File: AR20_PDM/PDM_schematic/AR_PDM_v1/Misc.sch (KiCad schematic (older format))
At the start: 91 parts, among them SW1 SW_DIP_x07, SW2 SW_Push, U13 Fet-P, U14 Fet-P, U15 Fet-P, U16 Fet-P, U17 Fet-P, U18 Fet-P, U19 Fet-P, U20 Fet-P, U21 Fet-P, U22 Fet-P, U23 Fet-P, U24 Fet-P, U25 Fet-P, U26 Fet-P, U27 Fet-P, U28 Fet-P, U29 Fet-P, U30 Fet-P, U31 Fet-P

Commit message: Alpha version DONE! - Gerber files generated
- Tweeked
- checked and re cheked
- added all missing components
- Created a really nice silkscreen
- Ready To Test
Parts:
- removed SW2: SW_Push, Connector_JST:JST_EH_B2B-EH-A_1x02_P2.50mm_Vertical, symbol Switch:SW_Push
- added P1: B4B-PH-SM4-TB, AR_PDM_v1:JST_B4B-PH-SM4-TB, symbol AR20_PDM_v1-rescue:B4B-PH-SM4-TB
- added R88: somthing_K_something, Resistor_SMD:R_0603_1608Metric, symbol AR20_PDM_v1-rescue:R-Device
- D21: renamed from D23; value Shutdown_Circuit_Active -> Shutdown_Circuit_Supply
- renumbered D12 to D10, D13 to D11, D14 to D12, D15 to D13, D16 to D14, D17 to D15, D18 to D16, D19 to D17, D20 to D18, D21 to D19, D22 to D20, D31 to D22, D24 to D23, D25 to D24, D26 to D25, D27 to D26, D28 to D27, D29 to D28, D30 to D29, D7 to D5, D8 to D6, D9 to D7, D10 to D8, D11 to D9, R14 to R48, R15 to R49, R16 to R50, R17 to R51, R18 to R52, R19 to R53, R20 to R54, R21 to R55, R22 to R56, R23 to R57, R24 to R58, R25 to R59, R26 to R60, R27 to R61, R28 to R62, R29 to R63, R30 to R64, R31 to R65, R32 to R66, R33 to R67, R34 to R68, R35 to R69, R36 to R70, R37 to R71, R38 to R72, R39 to R73, R40 to R74, R41 to R75, R42 to R76, R59 to R77, R43 to R78, R44 to R79, R45 to R80, R46 to R81, R47 to R82, R48 to R83, R49 to R84, R50 to R85, R51 to R86, R52 to R87, R54 to R89, R53 to R90, R55 to R91, R56 to R92, R57 to R93, U13 to U10, U14 to U11, U15 to U12, U16 to U13, U17 to U14, U18 to U15, U19 to U16, U20 to U17, U21 to U18, U22 to U19, U23 to U20, U24 to U21, U25 to U22, U26 to U23, U27 to U24, U28 to U25, U29 to U26, U30 to U27, U31 to U28
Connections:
- net GND: now also P1.4
- net Switch: now also P1.2
- net vcc_5v: now also P1.1, R88.2
- new net: P1.3, R88.1
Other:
- moved on the sheet: R90

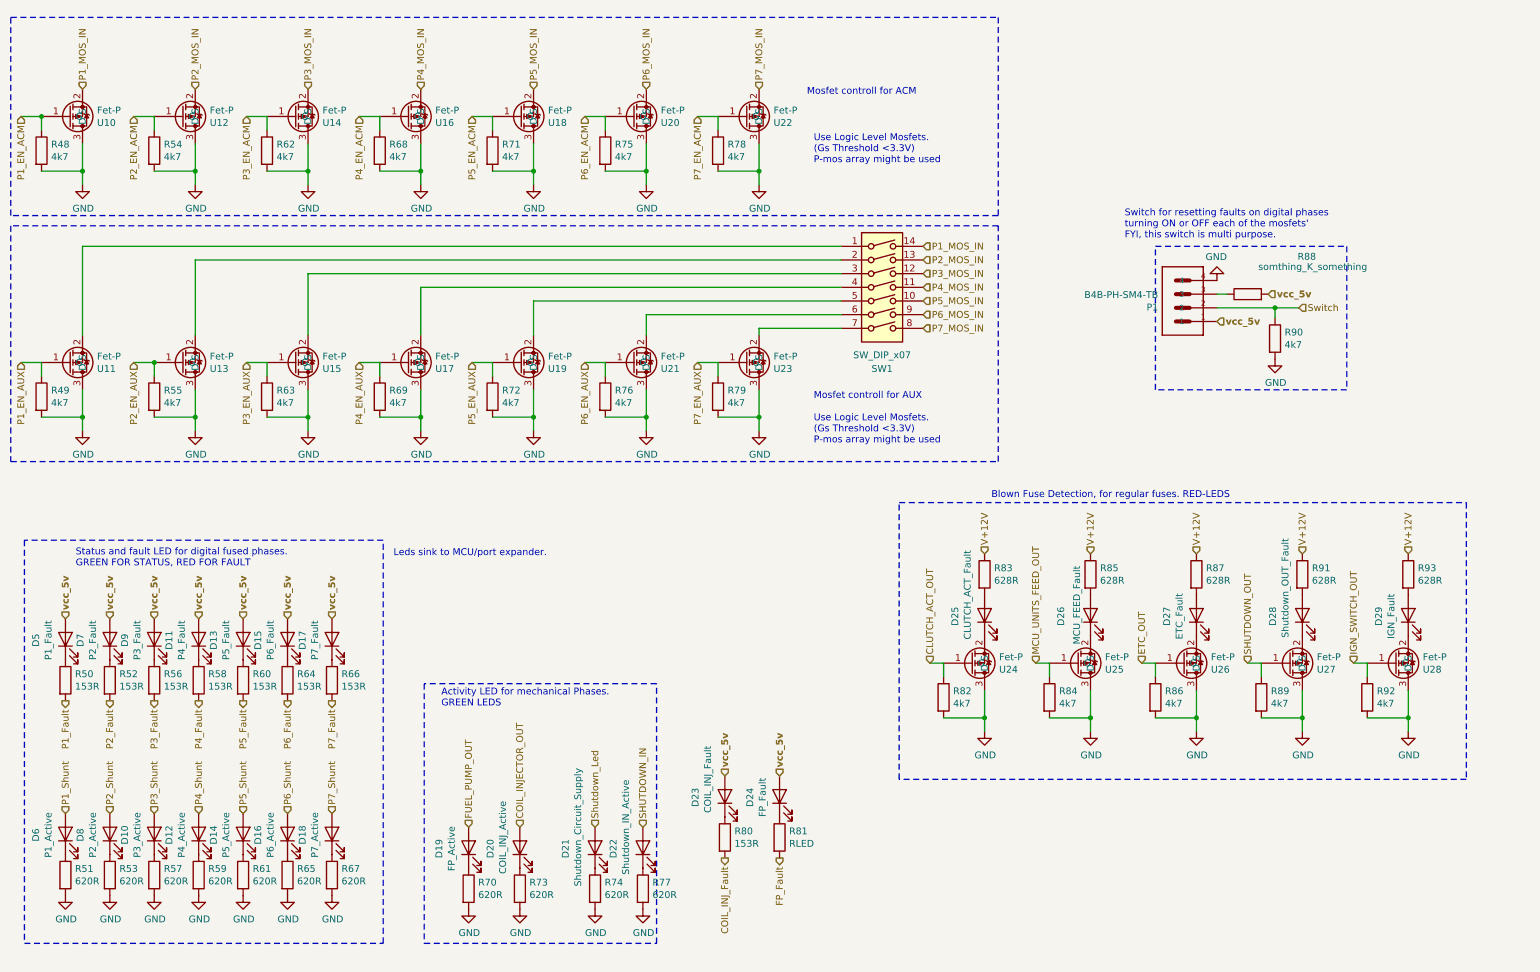
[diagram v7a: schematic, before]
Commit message: Fixed wrong resistors, mos sense. Gerber files updated
- removed all R_is_protection resistors on each mosfet line
- added one R_is_protection resistors to mos_sense_all
ps, mux N-fets, does not need overvoltage protection. 60 volt tolerant.
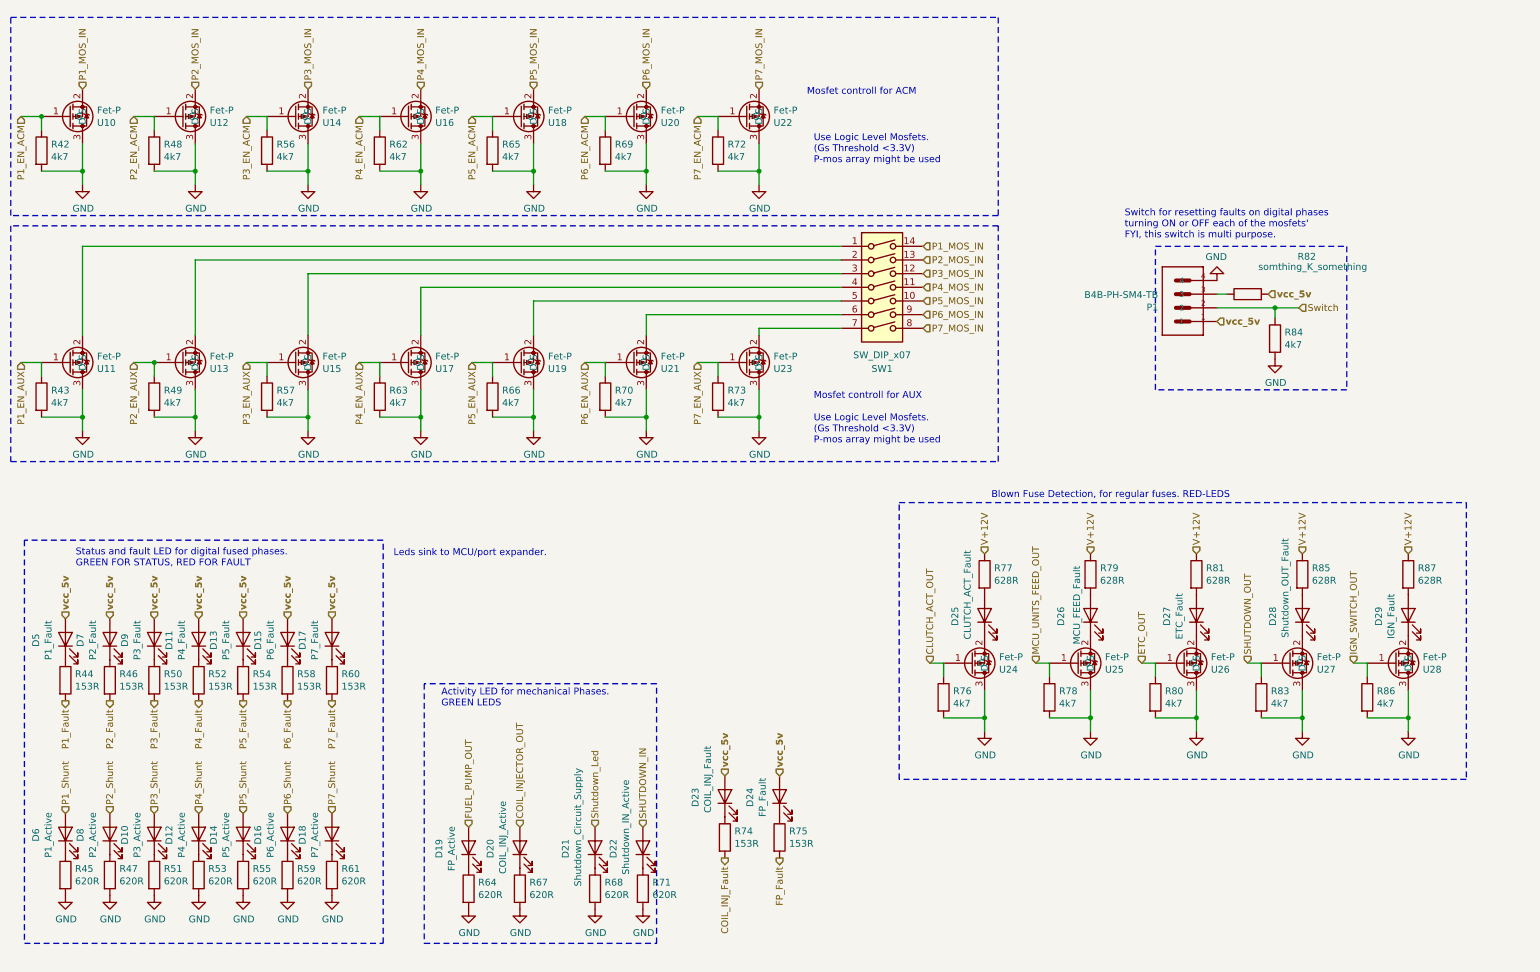
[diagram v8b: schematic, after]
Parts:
- R75: renamed from R81; value RLED -> 153R
- renumbered R48 to R42, R49 to R43, R50 to R44, R51 to R45, R52 to R46, R53 to R47, R54 to R48, R55 to R49, R56 to R50, R57 to R51, R58 to R52, R59 to R53, R60 to R54, R61 to R55, R62 to R56, R63 to R57, R64 to R58, R65 to R59, R66 to R60, R67 to R61, R68 to R62, R69 to R63, R70 to R64, R71 to R65, R72 to R66, R73 to R67, R74 to R68, R75 to R69, R76 to R70, R77 to R71, R78 to R72, R79 to R73, R80 to R74, R82 to R76, R83 to R77, R84 to R78, R85 to R79, R86 to R80, R87 to R81, R88 to R82, R89 to R83, R90 to R84, R91 to R85, R92 to R86, R93 to R87
